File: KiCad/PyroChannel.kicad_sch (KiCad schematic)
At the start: 5 parts, among them Q3 IRLML0030

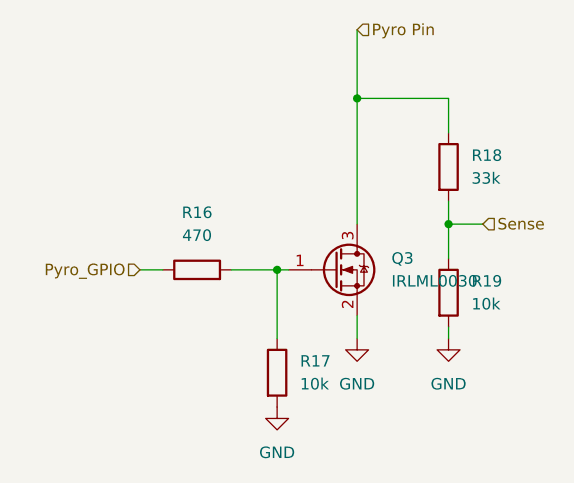
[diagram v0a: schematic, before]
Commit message: Switch added, LCSC table, other changes.
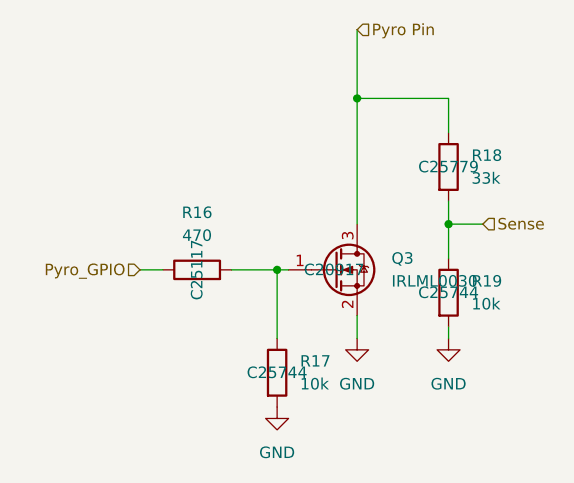
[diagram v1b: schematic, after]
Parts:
- Q3: LCSC (none) -> C20917
- R16: LCSC (none) -> C25117
- R17, R19: LCSC (none) -> C25744
- R18: LCSC (none) -> C25779
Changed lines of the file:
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@@
+			)
+		)
+		(property "LCSC" "C25779"
+			(at 157.48 82.55 0)
+			(effects
+				(font
+					(size 1.27 1.27)
+				)
 			)
 		)
@@
 			)
 		)
+		(property "LCSC" "C25117"
+			(at 129.54 93.98 0)
+			(effects
+				(font
+					(size 1.27 1.27)
+				)
+			)
+		)
 		(pin "2"
 		)
@@
 			)
 		)
+		(property "LCSC" "C20917"
+			(at 144.78 93.98 0)
+			(effects
+				(font
+					(size 1.27 1.27)
+				)
+			)
+		)
 		(pin "1"
 		)
@@
 			)
 		)
+		(property "LCSC" "C25744"
+			(at 138.43 105.41 0)
+			(effects
+				(font
+					(size 1.27 1.27)
+				)
+			)
+		)
 		(pin "2"
 		)
@@
 			)
 		)
+		(property "LCSC" "C25744"
+			(at 157.48 96.52 0)
+			(effects
+				(font
+					(size 1.27 1.27)
+				)
+			)
+		)
